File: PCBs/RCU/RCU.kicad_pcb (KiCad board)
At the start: 4 copper layers, 99 x 139 mm, 148 parts, among them J100 Conn_01x02, J200 USB_C_Receptacle_USB2.0, J201 Conn_01x05, J300 Right_Motor_Screw_Terminal, J301 Right_Encoder_Conn, J302 Left_Motor_Screw_Terminal, J303 Left_Encoder_Conn, J400 USB_C_Receptacle_USB2.0, Q400 2N7002NXAKR (NMOS), Q401 2N7002NXAKR (NMOS), Q402 BSS84AK,215 (PMOS), Q403 2N7002NXAKR (NMOS), SW201 SW_Push, SW400 SW_Push, SW401 SW_SPDT, U100 LM2576S-ADJ, U101 AP63203WU, U102 AZ1117-3.3, U200 STM32G0B1CBT6, U201 USBLC6-2SC6, U300 OPA320, U301 DRV8876, U302 OPA320, U303 DRV8876, U400 USBLC6-2SC6, U401 CH340C, U402 ESP32-MINI-1, U403 DG2788ADN-T1-GE4, U500 APDS-9306-065, U501 LSM6DS3, U502 SHT30-DIS, U600 ADC121C027CIMK/NOPB, U601 OPA320, U602 ADC121C027CIMK/NOPB, U603 OPA320, U700 SST26VF032BT-104I/SM, Y200 16MHz

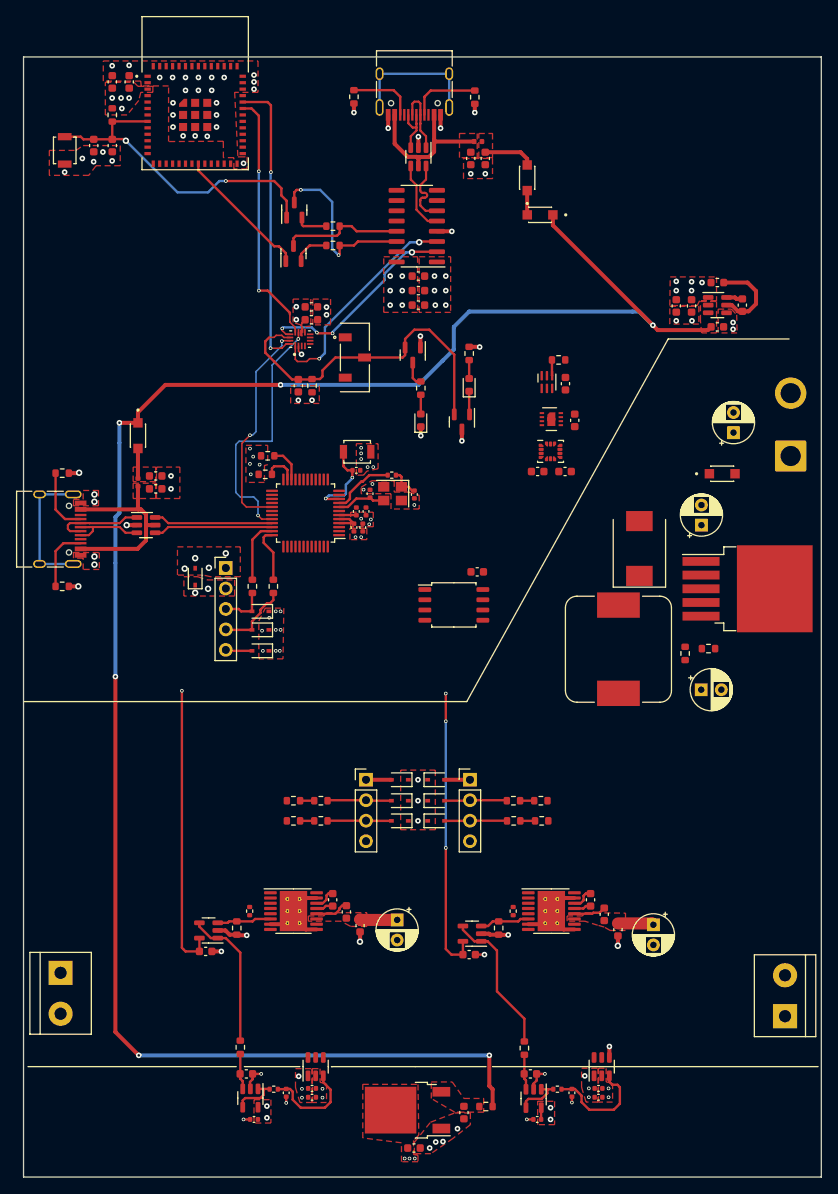
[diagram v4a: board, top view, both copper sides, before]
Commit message: Traced I2C lines
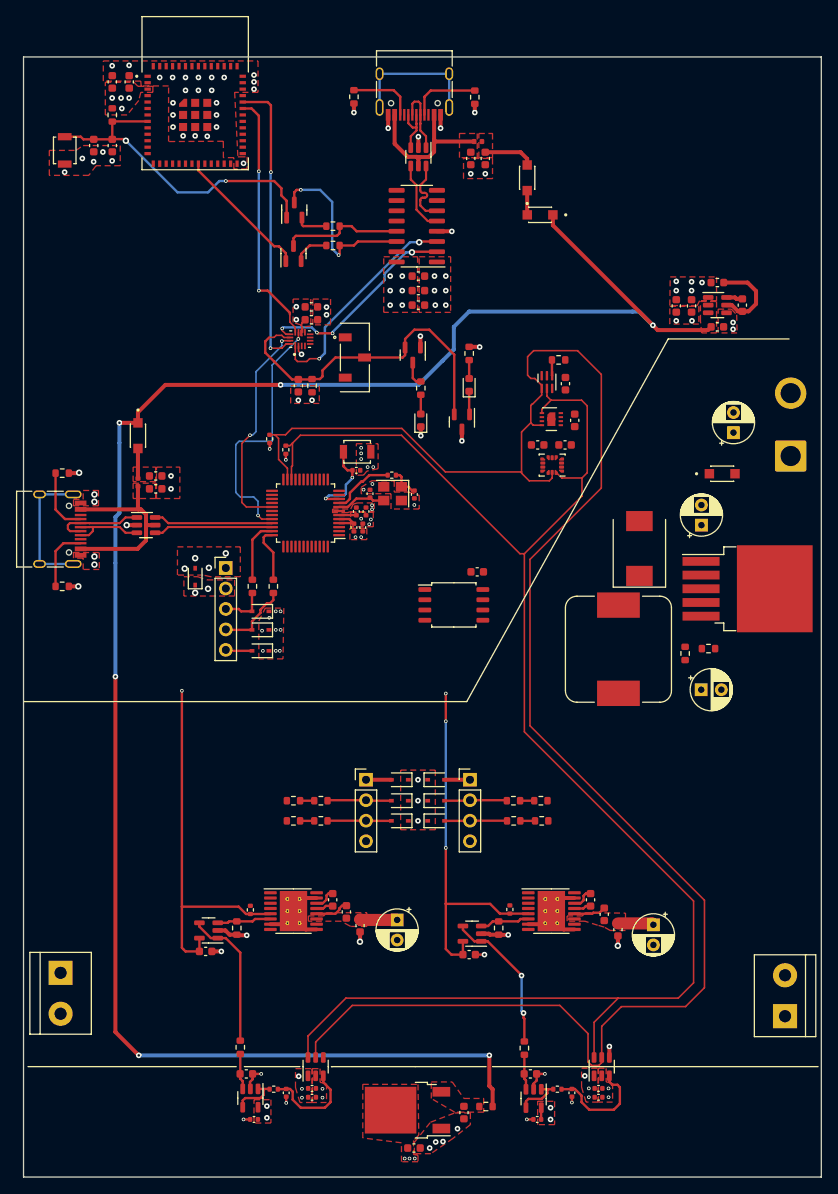
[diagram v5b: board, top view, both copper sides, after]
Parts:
- R201, R202: footprint Resistor_SMD:R_0603_1608Metric -> Resistor_SMD:R_0402_1005Metric
- moved C501 4.74 mm to (131.8, 69.2), turned to 180 degrees
- moved C502 4.74 mm to (135.2, 69.2), turned to 180 degrees
- moved R201 4.43 mm to (98.5, 68.4), turned to -90 degrees
- moved R202 2.37 mm to (100.5, 69.8), turned to -90 degrees
- moved U501 1.71 mm to (133.6, 71.7), turned to 180 degrees
- moved R300 0.46 mm to (128.3, 126.8)
- moved R306 0.17 mm to (96.2, 126.8)
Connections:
- R306 pad 1: +3V3 -> nFault_Left
- R306 pad 2: nFault_Left -> +3V3
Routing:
- net I2C_SCL: track 4.14 -> 226.3 mm
- net I2C_SDA: track 4.45 -> 198.2 mm
- net +3V3: track 84.1 -> 107.7 mm, vias 36 -> 33
- net Buffered_Right_Sensed_Motor_Current: vias 0 -> 2
- net GND: vias 107 -> 109

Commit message: Routed external memory
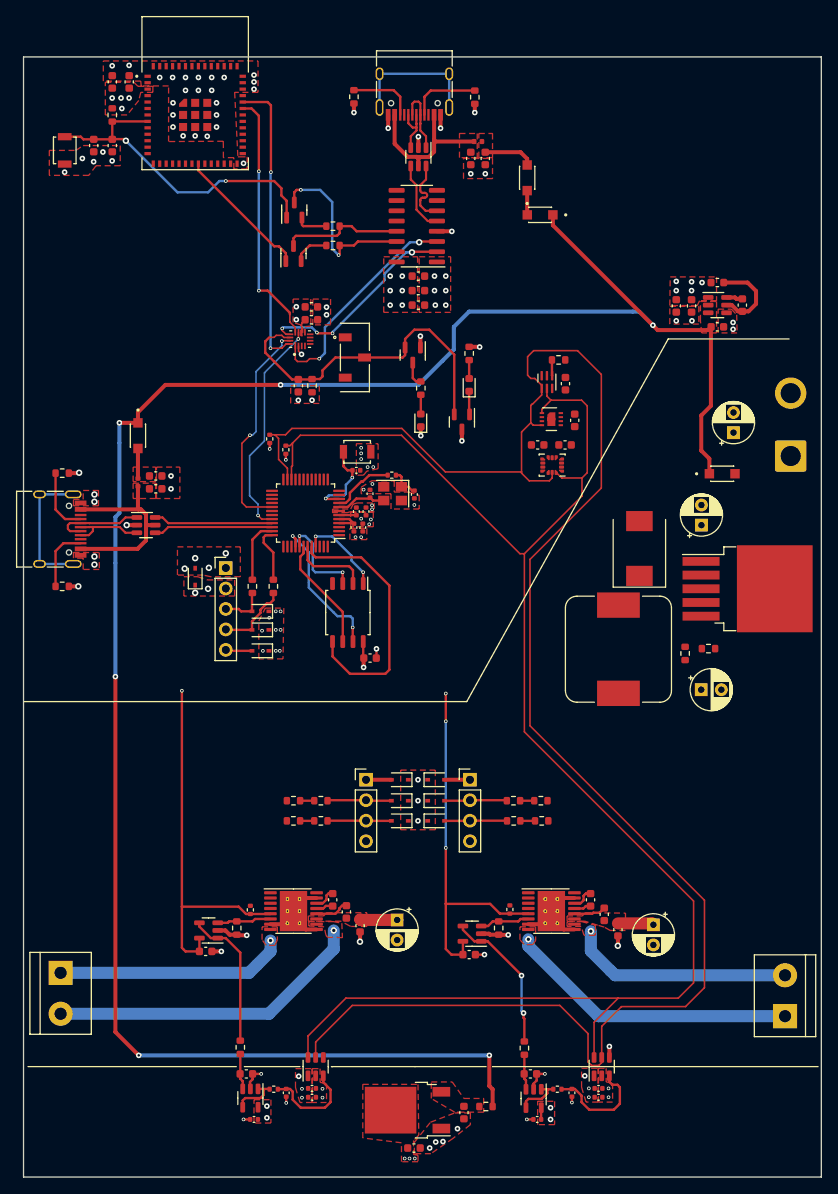
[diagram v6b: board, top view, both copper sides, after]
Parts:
- moved C700 17.1 mm to (111.0, 95.6), turned to 0 degrees
- moved U700 13.2 mm to (108.2, 90.0), turned to -90 degrees
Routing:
- net /[3] Motor_Control/Left_Out2: track 0.00 -> 39.5 mm, vias 0 -> 1
- net /[3] Motor_Control/Right_Out1: track 0.00 -> 36.3 mm, vias 0 -> 1
- net SPI_MOSI: track 0.00 -> 32.6 mm
- net /[3] Motor_Control/Left_Out1: track 0.00 -> 28.5 mm, vias 0 -> 1
- net /[3] Motor_Control/Right_Out2: track 0.00 -> 27.8 mm, vias 0 -> 1
- net VCOM: track 231.4 -> 250.6 mm
- net Hold: track 0.00 -> 18.6 mm, vias 0 -> 2
- net SPI_SCK: track 0.00 -> 14.1 mm
- net Write_Protect: track 0.00 -> 11.8 mm, vias 0 -> 2
- net Mem_Select: track 0.00 -> 10.8 mm, vias 0 -> 2
- net SPI_MISO: track 0.00 -> 9.50 mm
- net UART_MCU_TX: track 32.4 -> 27.6 mm
- net +3V3: track 107.7 -> 110.9 mm, vias 33 -> 34
- net GND: track 50.5 -> 51.6 mm, vias 109 -> 110
- added copper zone on F.Cu, net /[3] Motor_Control/Left_Out1
- added copper zone on F.Cu, net /[3] Motor_Control/Left_Out2
- added copper zone on F.Cu, net /[3] Motor_Control/Right_Out1
- added copper zone on F.Cu, net /[3] Motor_Control/Right_Out2

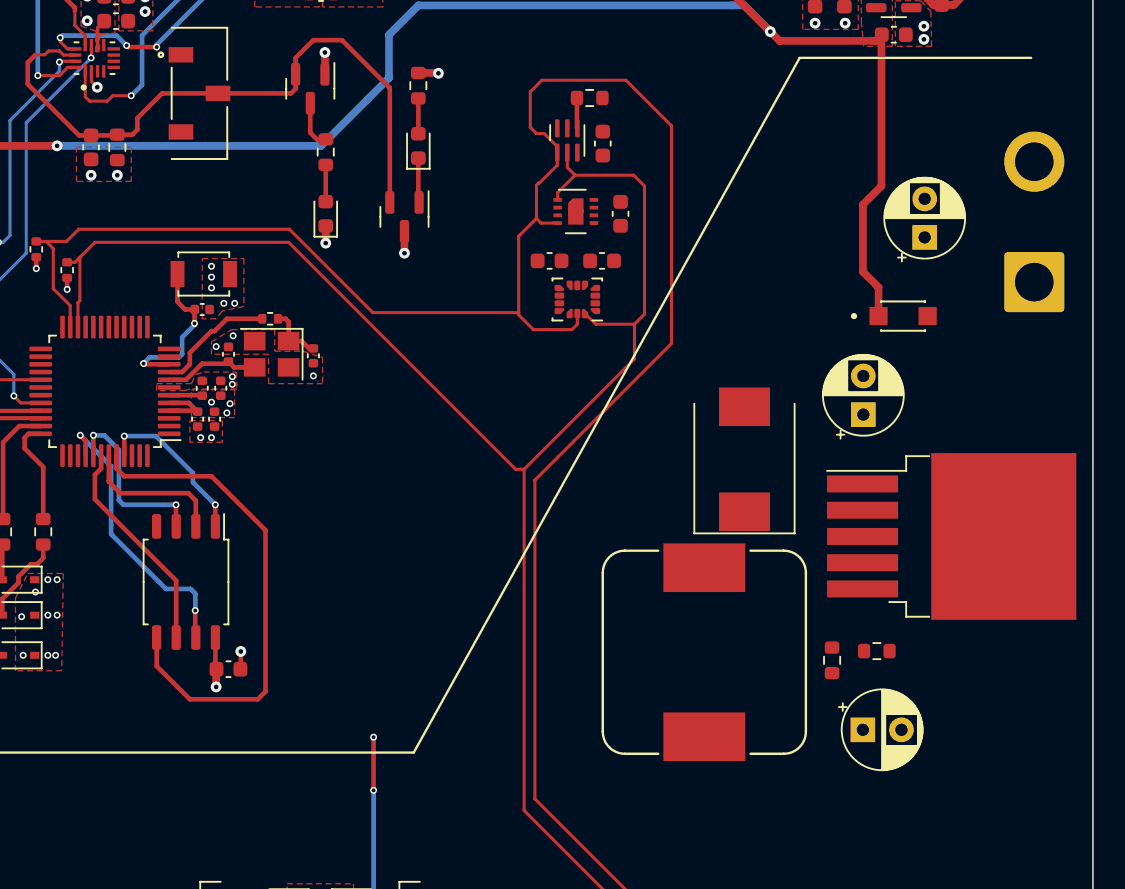
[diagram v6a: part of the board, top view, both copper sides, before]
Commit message: routed 6V regulator
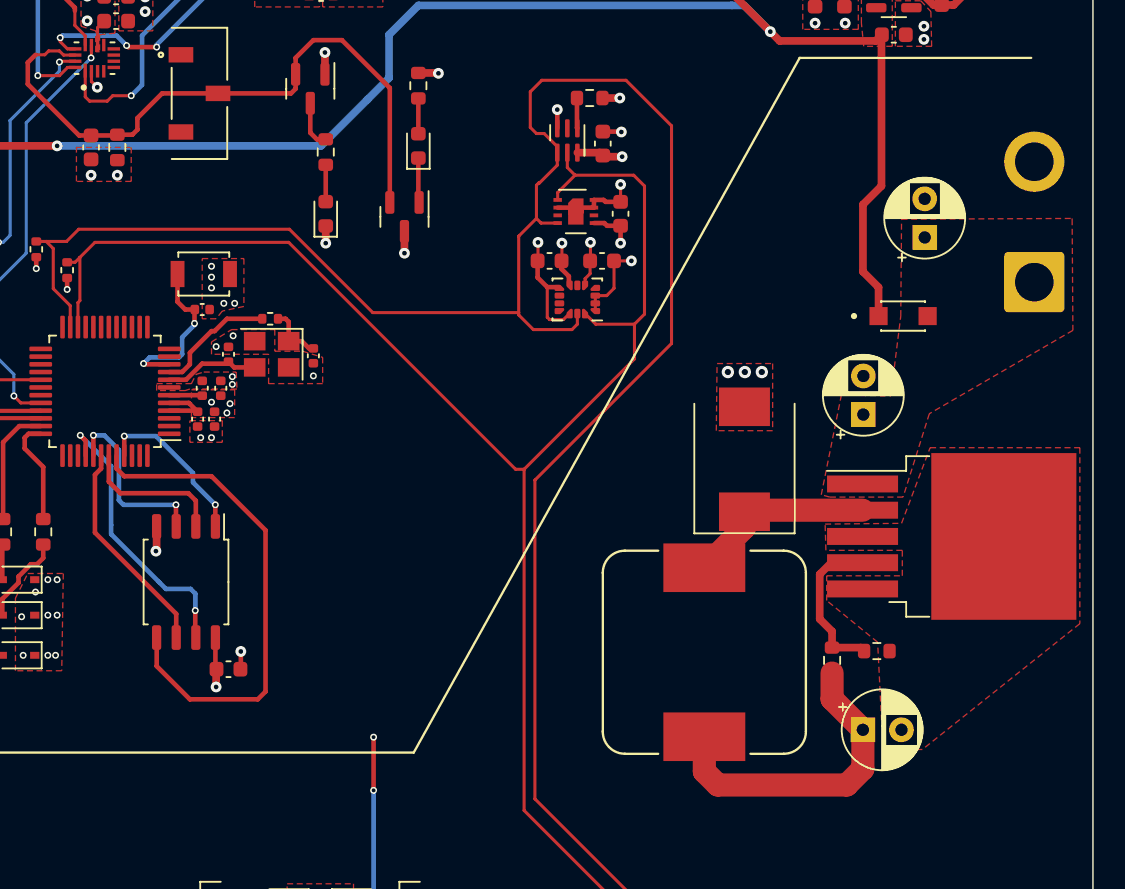
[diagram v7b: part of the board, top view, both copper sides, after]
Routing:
- net +6V: track 15.4 -> 35.7 mm
- net GND: track 51.6 -> 69.9 mm, vias 110 -> 119
- net +3V3: track 110.9 -> 128.5 mm, vias 34 -> 39
- net /[1] Power/BUCK_OUT_104: track 0.00 -> 12.4 mm
- net /[1] Power/BUCK_FB_104: track 0.00 -> 10.3 mm
- added copper zone on F.Cu, net +BATT

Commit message: Finished routing and change signals layers to mixed
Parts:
- turned R306 to -90 degrees
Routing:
- net Awake_Sleep: track 0.00 -> 112.2 mm, vias 0 -> 5
- net Control_Input_Mode: track 0.00 -> 87.1 mm, vias 0 -> 6
- net Right_Enable/PWM: track 0.00 -> 77.5 mm, vias 0 -> 4
- net Right_Phase/PWM: track 0.00 -> 76.3 mm, vias 0 -> 4
- net Left_Phase/PWM: track 0.00 -> 74.4 mm, vias 0 -> 4
- net nFault_Right: track 0.00 -> 63.0 mm, vias 0 -> 2
- net Right_Wheel_Encoder_B: track 1.82 -> 64.7 mm, vias 0 -> 2
- net nFault_Left: track 0.00 -> 59.1 mm, vias 0 -> 4
- net Left_Enable/PWM: track 0.00 -> 58.9 mm, vias 0 -> 2
- net /[2] Microcontroller/NRST: track 14.1 -> 71.7 mm, vias 2 -> 4
- net Left_Wheel_Encoder_B: track 1.75 -> 55.2 mm, vias 0 -> 2
- net Right_Wheel_Encoder_A: track 1.75 -> 52.3 mm, vias 0 -> 2
- net Left_Wheel_Encoder_A: track 1.75 -> 48.0 mm, vias 0 -> 2
- net GND: track 69.9 -> 74.5 mm, vias 119 -> 123
- net +3V3: track 128.5 -> 129.9 mm, vias 39 -> 40
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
